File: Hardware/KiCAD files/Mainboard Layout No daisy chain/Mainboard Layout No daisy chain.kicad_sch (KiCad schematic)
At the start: 90 parts, among them J10 Conn_01x02, J11 Conn_01x04, J12 JST_06, J13 Conn_01x08, J14 Conn_01x08, J15 Screw_Terminal_2_P5.00mm, J17 PINHD_1x8_Male, J18 PINHD_1x8_Male, J19 PINHD_1x8_Male, J2 Screw_Terminal_2_P5.00mm, J20 PINHD_1x8_Male, J22 PINHD_1x8_Male, J23 PINHD_1x8_Male, J24 PINHD_1x8_Male, J25 Conn_01x04, J26 Conn_01x04, J27 Conn_01x04, J28 PINHD_1x8_Male, J3 Screw_Terminal_2_P3.50mm, J30 USB-A1VSB6, J31 JST_03, J32 USB-A1VSB6, J34 JST_03, J35 JST_03, J36 JST_03, J37 JST_03, J38 JST_03, J4 JST_06, J5 Conn_01x04, J6 JST_06, J7 JST_06, J8 Conn_01x06, J9 Conn_01x10, Q1 BS170, Q2 2DD1664, SW1 210-4MS, SW2 210-4MS, SW3 210-4MS, SW4 210-4MS, SW8 Push_Button, SW9 Push_Button, U1 CP2102-GM, U12 ESP32-S3-WROOM-1, U2 PCA9534PW_118, U4 PCA9534PW_118

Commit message: part of the way through next iteration
Non-daisy chain Mainboard is ~50% through
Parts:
- removed J10: Conn_01x02, PCM_SparkFun-Connector:1x02_P2.54mm, symbol PCM_SparkFun-Connector:Conn_01x02_P2.54mm
- removed J8: Conn_01x06, PCM_SparkFun-Connector:1x06_P2.54mm, symbol PCM_SparkFun-Connector:Conn_01x06_P2.54mm
- added J1: JST_03, Connector_JST:JST_EH_B3B-EH-A_1x03_P2.50mm_Vertical, symbol PCM_SL_Connectors:JST_03
- R50: footprint PCM_SparkFun-Resistor:R_0603_1608Metric -> Resistor_THT:R_Axial_DIN0207_L6.3mm_D2.5mm_P10.16mm_Horizontal
- U1: footprint CP2102:QFN28_5X5_SIL -> cp2102 V1:QFN28_5X5_SIL
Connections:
- net CHAINL0_MISO_1 is gone; now on net MOSI_1: J13.5 (Pin_5), J14.7 (Pin_7)
- net CHAINL0_MISO_4 is gone; now on net MOSI_4: J9.9 (Pin_9)
- net STEPE: now also U4.7 (IO3); no longer U4.4 (IO0)
- net Suspend: now also U4.4 (IO0); no longer U4.7 (IO3)
- net SPI4_0SS: now reaches U4.12 (IO7)
- net at U12.7 (GPIO7/TOUCH7/ADC1_CH6): now also J1.1
- net at U12.17 (GPIO9/TOUCH9/ADC1_CH8/FSPIHD/SUBSPIHD): now also J1.2
- net SPI1_0SS: now reaches U2.11 (IO6)
- net SPI1_0SS: now also J13.6 (Pin_6), J14.4 (Pin_4)
- removed net SPI1_CS: J13.6 (Pin_6), J14.4 (Pin_4), U12.12 (GPIO8/TOUCH8/ADC1_CH7/SUBSPICS1)
- net SPI4_CS: no longer names the net of U12.18 (GPIO10/TOUCH10/ADC1_CH9/FSPICS0/FSPIIO4/SUBSPICS0)
- net SPI4_CS: no longer J9.3 (Pin_3)
- new net SPI4_1SS: J9.3 (Pin_3), U12.12 (GPIO8/TOUCH8/ADC1_CH7/SUBSPICS1)
- no-connect marks 34 -> 32

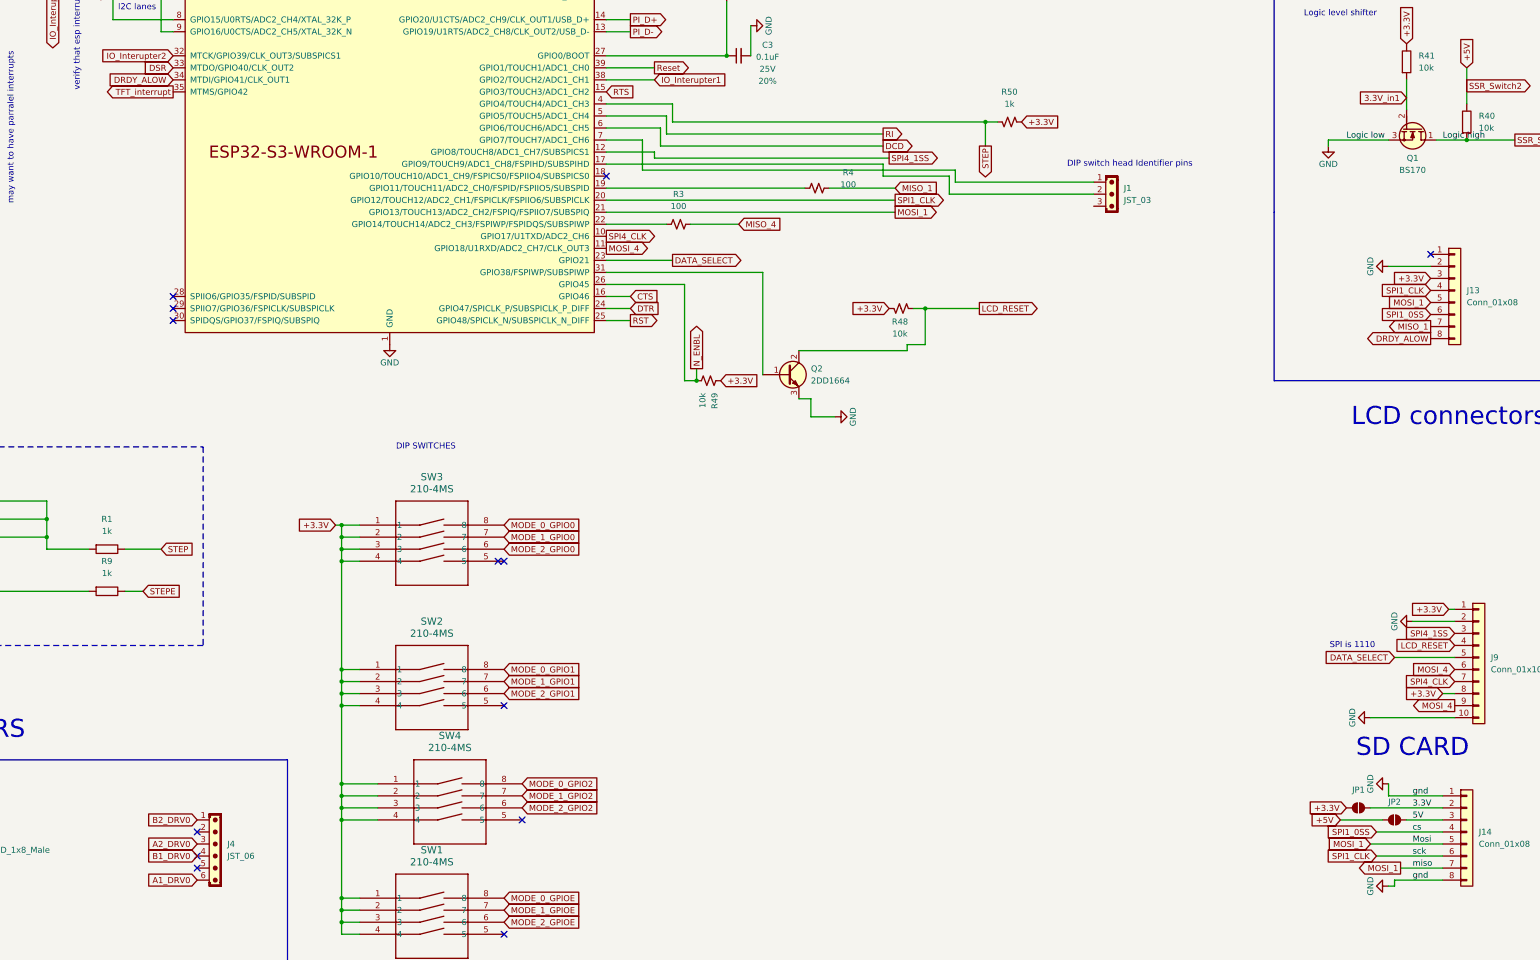
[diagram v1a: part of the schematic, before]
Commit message: 1st submitted iteration
added a folder for reviewing PCB's.
fixed various smaller issues on the PCB.
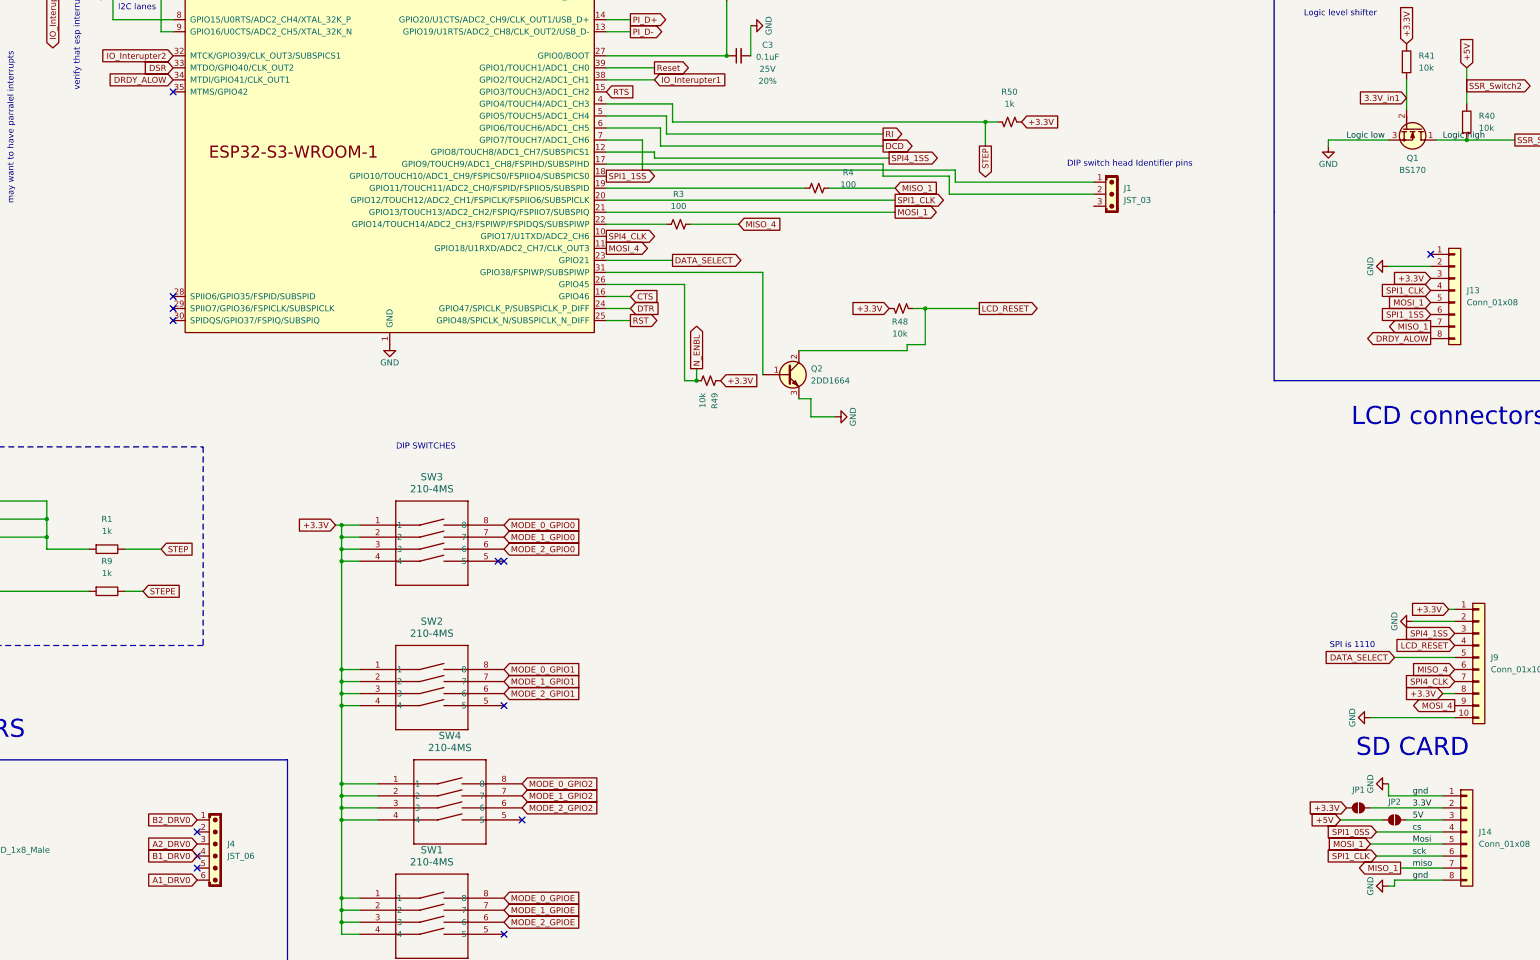
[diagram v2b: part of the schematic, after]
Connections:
- net MISO_1: now also J14.7 (Pin_7)
- net MISO_4: now also J9.6 (Pin_6)
- net MOSI_1: no longer J14.7 (Pin_7)
- net MOSI_4: no longer J9.6 (Pin_6)
- net SPI1_0SS: no longer J13.6 (Pin_6)
- net SPI1_1SS: now reaches U12.18 (GPIO10/TOUCH10/ADC1_CH9/FSPICS0/FSPIIO4/SUBSPICS0)
- net SPI1_1SS: now also J13.6 (Pin_6)
- net TFT_interrupt: no longer names the net of U12.35 (MTMS/GPIO42)
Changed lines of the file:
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@@
 	)
 	(no_connect
-		(at 264.16 105.41)
+		(at 72.39 125.73)
 	)
 	(no_connect
-		(at 72.39 125.73)
+		(at 172.72 87.63)
 	)
 	(no_connect
@@
 		)
 	)
-	(global_label "SPI1_0SS"
+	(global_label "SPI1_1SS"
 		(shape input)
 		(at 438.15 134.62 180)
@@
 		)
 	)
-	(global_label "MOSI_4"
+	(global_label "MISO_4"
 		(shape input)
 		(at 443.23 209.55 180)
@@
 		)
 	)
-	(global_label "TFT_interrupt"
-		(shape output)
-		(at 172.72 87.63 180)
-		(fields_autoplaced yes)
-		(effects
-			(font
-				(size 1.27 1.27)
-			)
-			(justify right)
-		)
-		(property "Intersheetrefs" "${INTERSHEET_REFS}"
-			(at 157.5792 87.63 0)
-			(hide yes)
-			(show_name no)
-			(do_not_autoplace no)
-			(effects
-				(font
-					(size 1.27 1.27)
-				)
-				(justify right)
-			)
-		)
-	)
 	(global_label "PI_D-"
 		(shape input)
@@
 		)
 	)
+	(global_label "SPI1_1SS"
+		(shape output)
+		(at 264.16 105.41 0)
+		(fields_autoplaced yes)
+		(effects
+			(font
+				(size 1.27 1.27)
+			)
+			(justify left)
+		)
+		(property "Intersheetrefs" "${INTERSHEET_REFS}"
+			(at 276.0351 105.41 0)
+			(hide yes)
+			(show_name no)
+			(do_not_autoplace no)
+			(effects
+				(font
+					(size 1.27 1.27)
+				)
+				(justify left)
+			)
+		)
+	)
 	(global_label "SSR_Switch2"
 		(shape input)
@@
 		)
 	)
-	(global_label "MOSI_1"
+	(global_label "MISO_1"
 		(shape output)
 		(at 431.8 251.46 180)
